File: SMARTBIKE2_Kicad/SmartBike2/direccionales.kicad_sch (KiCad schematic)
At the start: 9 parts, among them Q3 SI2302, Q4 SI2302, U2 NA555D

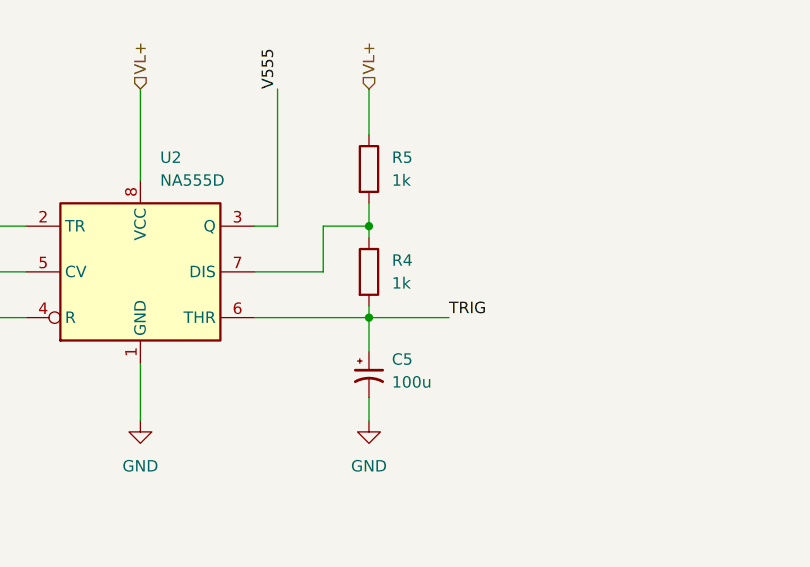
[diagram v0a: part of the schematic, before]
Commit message: Alimentación ESP32
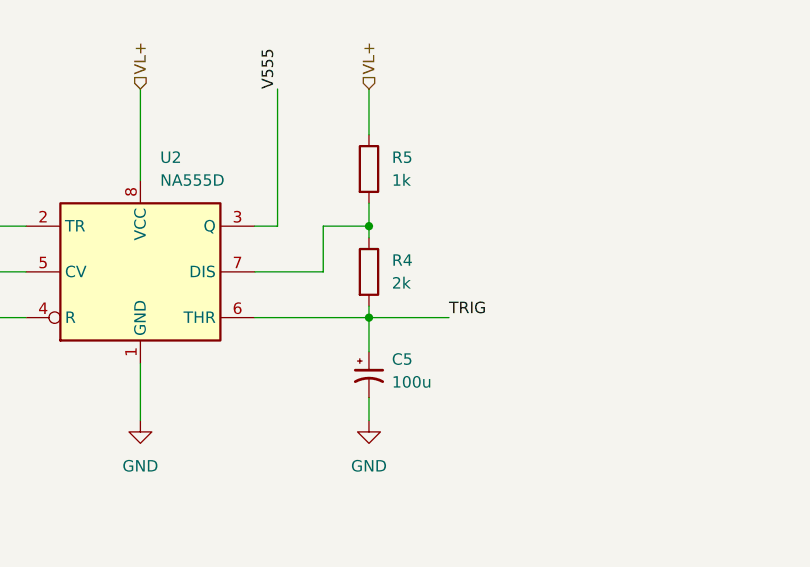
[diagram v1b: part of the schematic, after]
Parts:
- R4: value 1k -> 2k
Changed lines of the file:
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@@
       (effects (font (size 1.27 1.27)) (justify left))
     )
-    (property "Value" "1k" (at 106.68 60.96 0)
+    (property "Value" "2k" (at 106.68 60.96 0)
       (effects (font (size 1.27 1.27)) (justify left))
     )

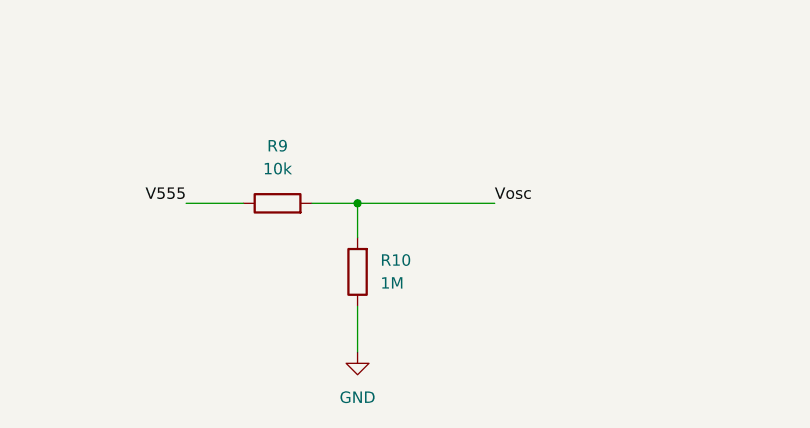
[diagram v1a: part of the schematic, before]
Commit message: Alarma, luces frontales y modulos
+ Circuito luces frontales
+ Conector Luces
+ Conector GPS
+ Conector SIM
+ Conector acelerómetro

~ Acondicionamiento ESP32
~ Huellas
~ PCB
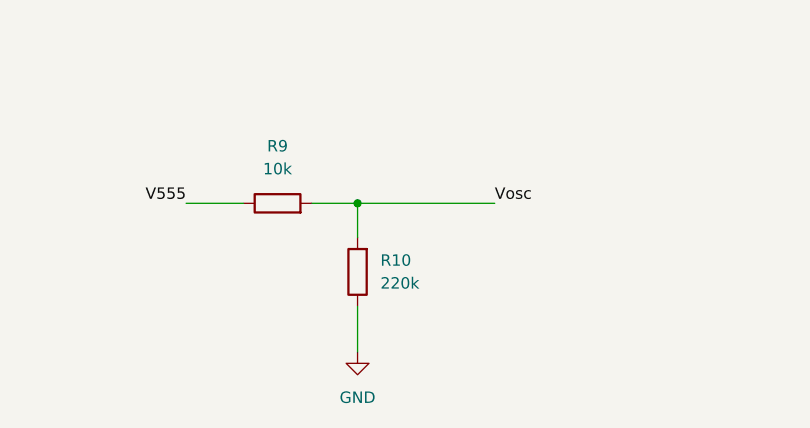
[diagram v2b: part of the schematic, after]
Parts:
- R10: value 1M -> 220k
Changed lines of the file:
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@@
       (effects (font (size 1.27 1.27)) (justify right))
     )
-    (property "Value" "1M" (at 83.82 139.7 0)
+    (property "Value" "220k" (at 83.82 139.7 0)
       (effects (font (size 1.27 1.27)) (justify right))
     )

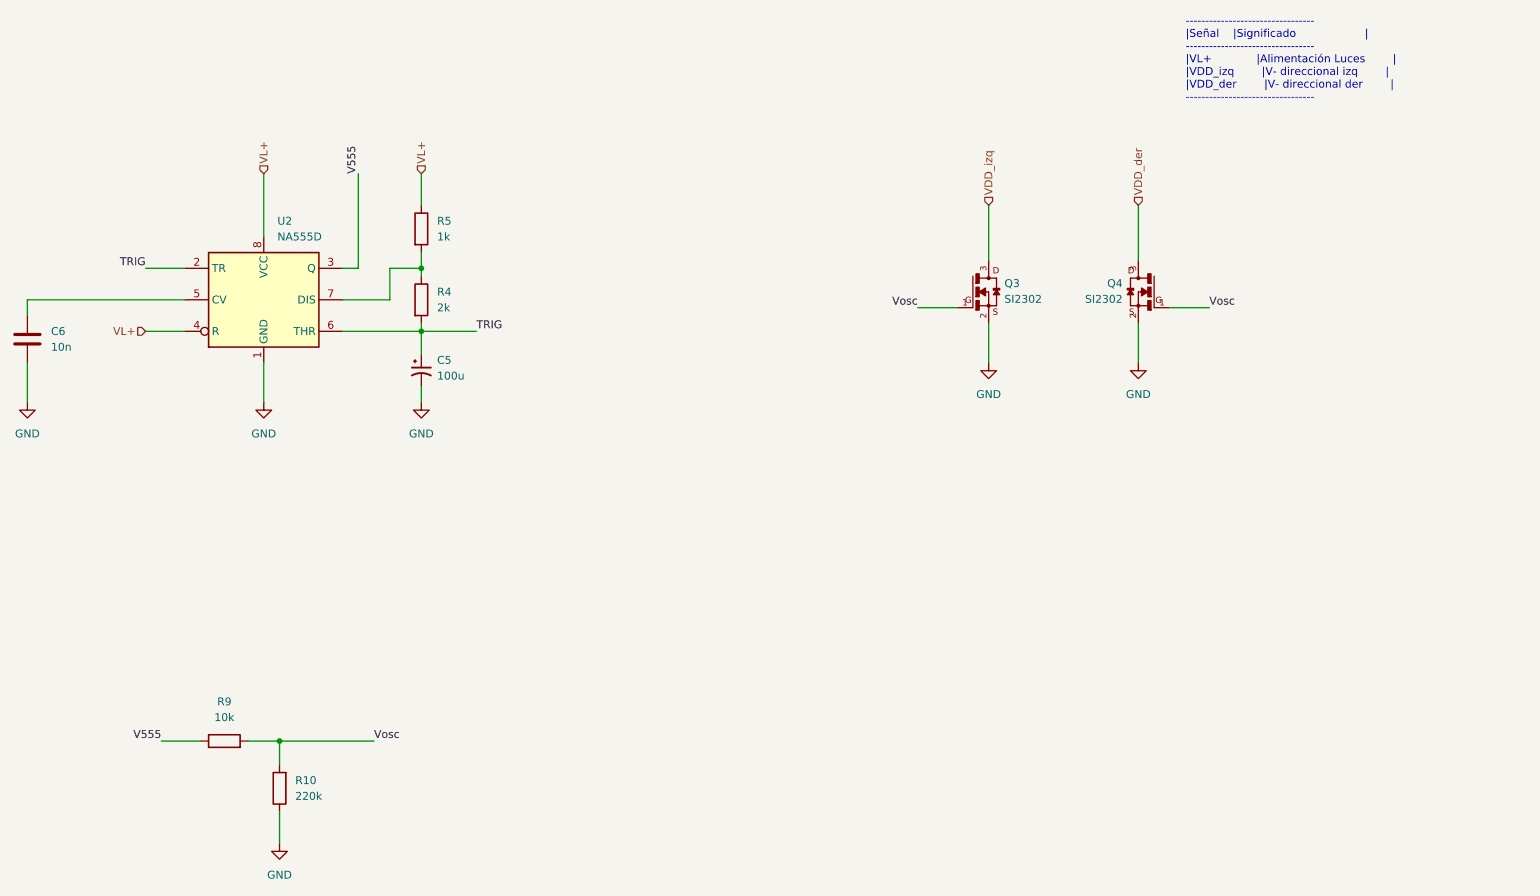
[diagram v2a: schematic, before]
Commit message: Beta 100% esquemáticos
+ Acondicionamiento ESP32

~ Huellas
~ PCB
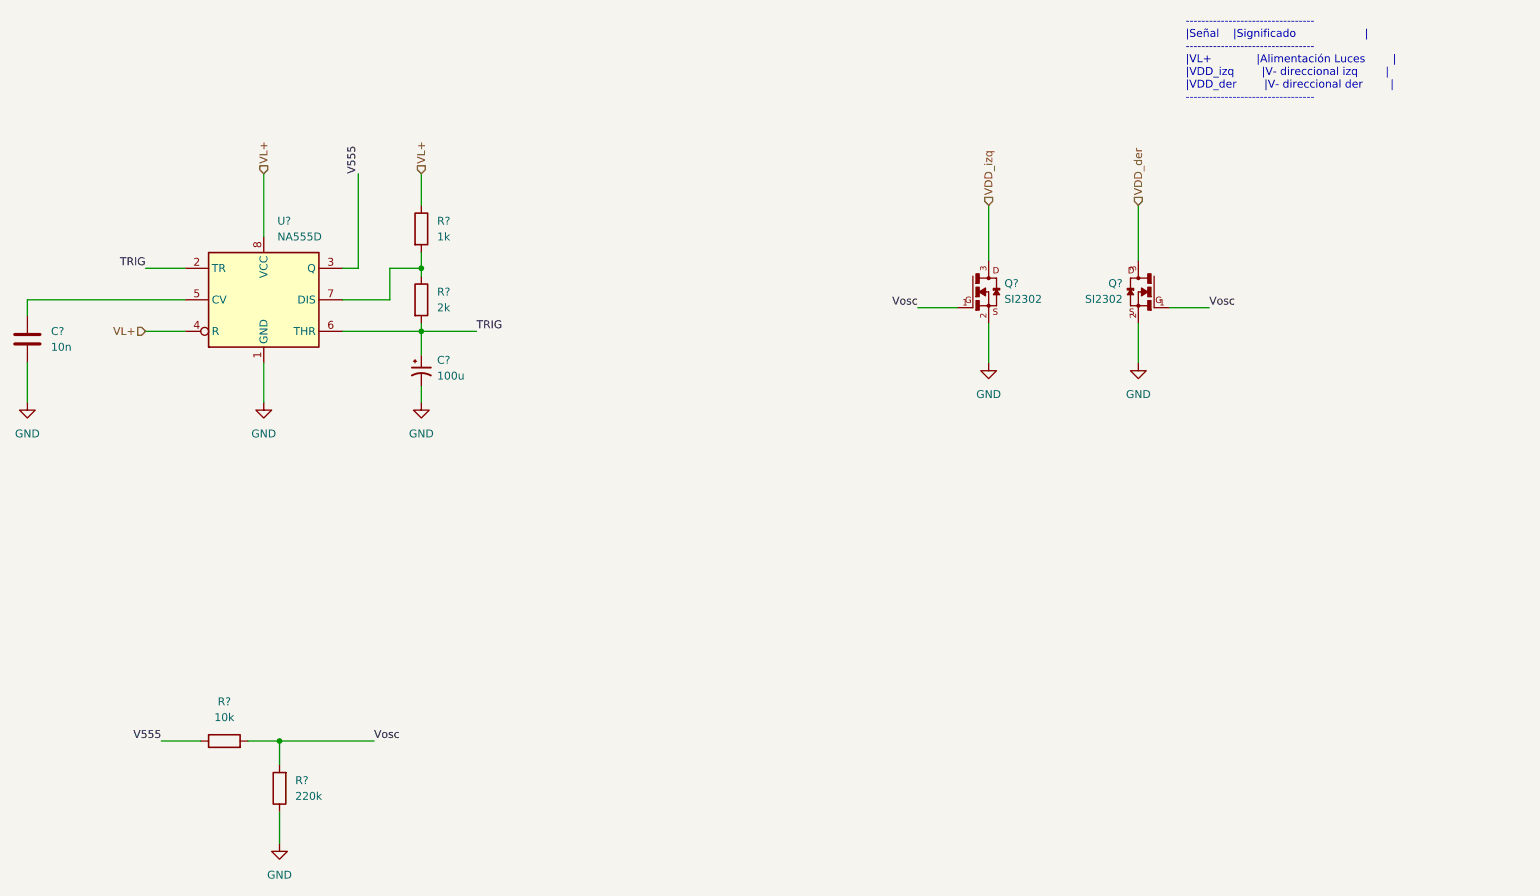
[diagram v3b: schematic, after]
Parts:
- renumbered C6 to C?, C5 to C?, Q4 to Q?, Q3 to Q?, R5 to R?, R10 to R?, R9 to R?, R4 to R?, U2 to U?

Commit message: cache
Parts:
- C?: footprint (none) -> Capacitor_SMD:C_0805_2012Metric_Pad1.18x1.45mm_HandSolder
- C?: footprint (none) -> Capacitor_SMD:CP_Elec_6.3x5.4
- Q? (x2): footprint SI2302:SOT23 -> Package_TO_SOT_SMD:SOT-23
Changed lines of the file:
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@@
       (effects (font (size 1.27 1.27)) (justify left))
     )
-    (property "Footprint" "" (at 41.6052 69.85 0)
+    (property "Footprint" "Capacitor_SMD:C_0805_2012Metric_Pad1.18x1.45mm_HandSolder" (at 41.6052 69.85 0)
       (effects (font (size 1.27 1.27)) hide)
     )
@@
       (effects (font (size 1.27 1.27)) (justify left))
     )
-    (property "Footprint" "SI2302:SOT23" (at 219.71 58.42 0)
+    (property "Footprint" "Package_TO_SOT_SMD:SOT-23" (at 219.71 58.42 0)
       (effects (font (size 1.27 1.27)) (justify bottom) hide)
     )
@@
       (effects (font (size 1.27 1.27)) (justify left))
     )
-    (property "Footprint" "" (at 104.14 71.12 0)
+    (property "Footprint" "Capacitor_SMD:CP_Elec_6.3x5.4" (at 104.14 71.12 0)
       (effects (font (size 1.27 1.27)) hide)
     )
@@
       (effects (font (size 1.27 1.27)) (justify left))
     )
-    (property "Footprint" "SI2302:SOT23" (at 195.58 58.42 0)
-      (effects (font (size 1.27 1.27)) (justify bottom) hide)
-    )
+    (property "Footprint" "Package_TO_SOT_SMD:SOT-23" (at 195.58 58.42 0)
+      (effects (font (size 1.27 1.27)) (justify bottom) hide)
+    )

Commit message: Mas huellas
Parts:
- R? (x4): footprint (none) -> Resistor_SMD:R_0805_2012Metric_Pad1.20x1.40mm_HandSolder
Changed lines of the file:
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@@
       (effects (font (size 1.27 1.27)) (justify left))
     )
-    (property "Footprint" "" (at 102.362 48.26 90)
+    (property "Footprint" "Resistor_SMD:R_0805_2012Metric_Pad1.20x1.40mm_HandSolder" (at 102.362 48.26 90)
       (effects (font (size 1.27 1.27)) hide)
     )
@@
       (effects (font (size 1.27 1.27)) (justify right))
     )
-    (property "Footprint" "" (at 83.058 138.43 90)
+    (property "Footprint" "Resistor_SMD:R_0805_2012Metric_Pad1.20x1.40mm_HandSolder" (at 83.058 138.43 90)
       (effects (font (size 1.27 1.27)) hide)
     )
@@
       (effects (font (size 1.27 1.27)))
     )
-    (property "Footprint" "" (at 72.39 132.588 90)
+    (property "Footprint" "Resistor_SMD:R_0805_2012Metric_Pad1.20x1.40mm_HandSolder" (at 72.39 132.588 90)
       (effects (font (size 1.27 1.27)) hide)
     )
@@
       (effects (font (size 1.27 1.27)) (justify left))
     )
-    (property "Footprint" "" (at 102.362 59.69 90)
-      (effects (font (size 1.27 1.27)) hide)
-    )
+    (property "Footprint" "Resistor_SMD:R_0805_2012Metric_Pad1.20x1.40mm_HandSolder" (at 102.362 59.69 90)
+      (effects (font (size 1.27 1.27)) hide)
+    )
